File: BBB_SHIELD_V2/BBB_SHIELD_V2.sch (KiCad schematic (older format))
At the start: 6 parts, among them J1 Screw_Terminal_01x04

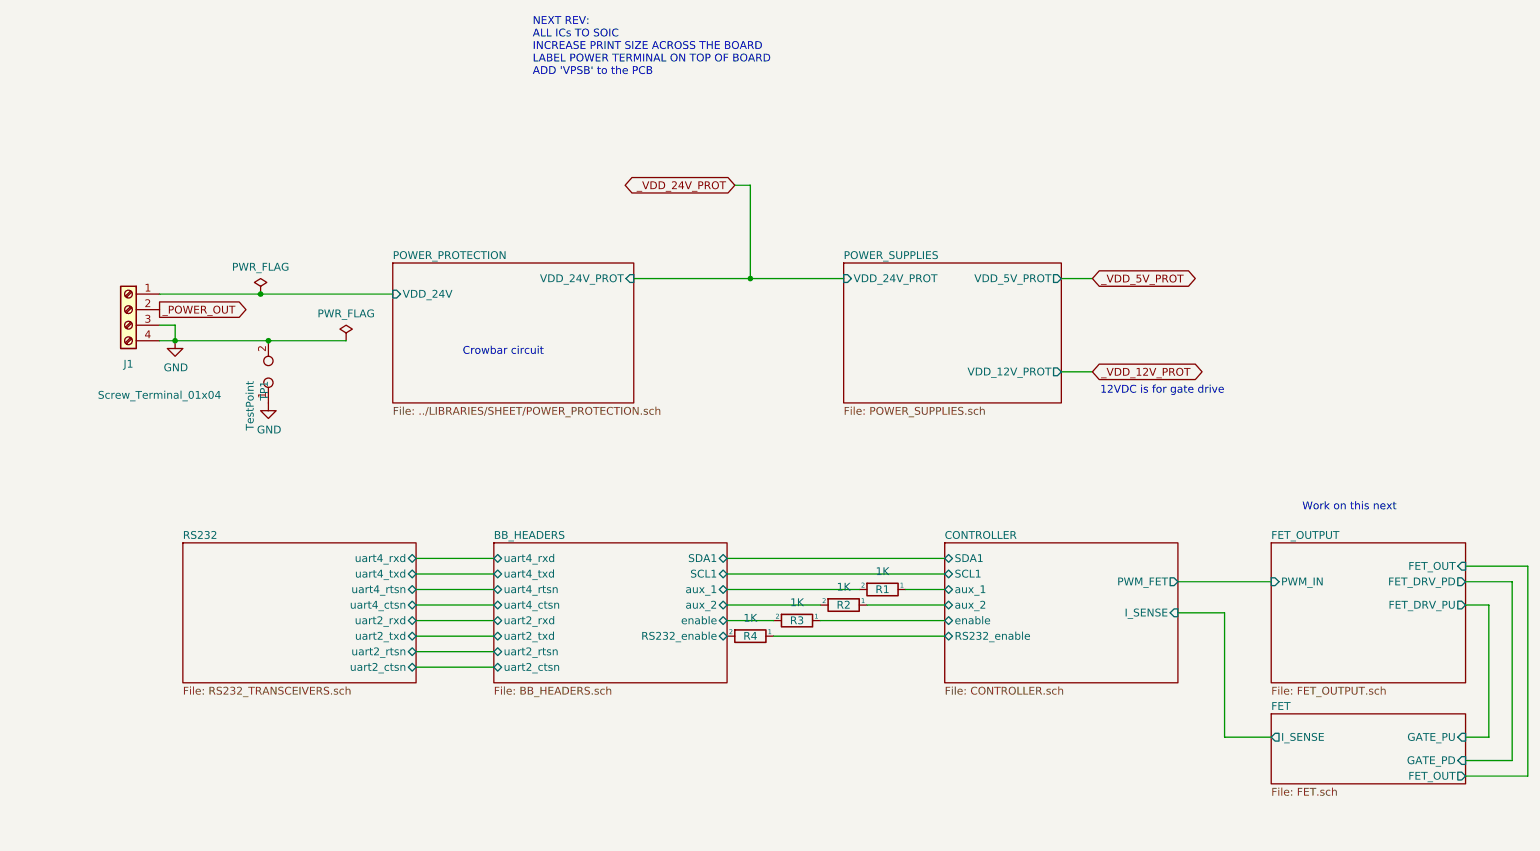
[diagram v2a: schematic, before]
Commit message: Schematics cleanup.  Gerbers for the latest manufacturing release.
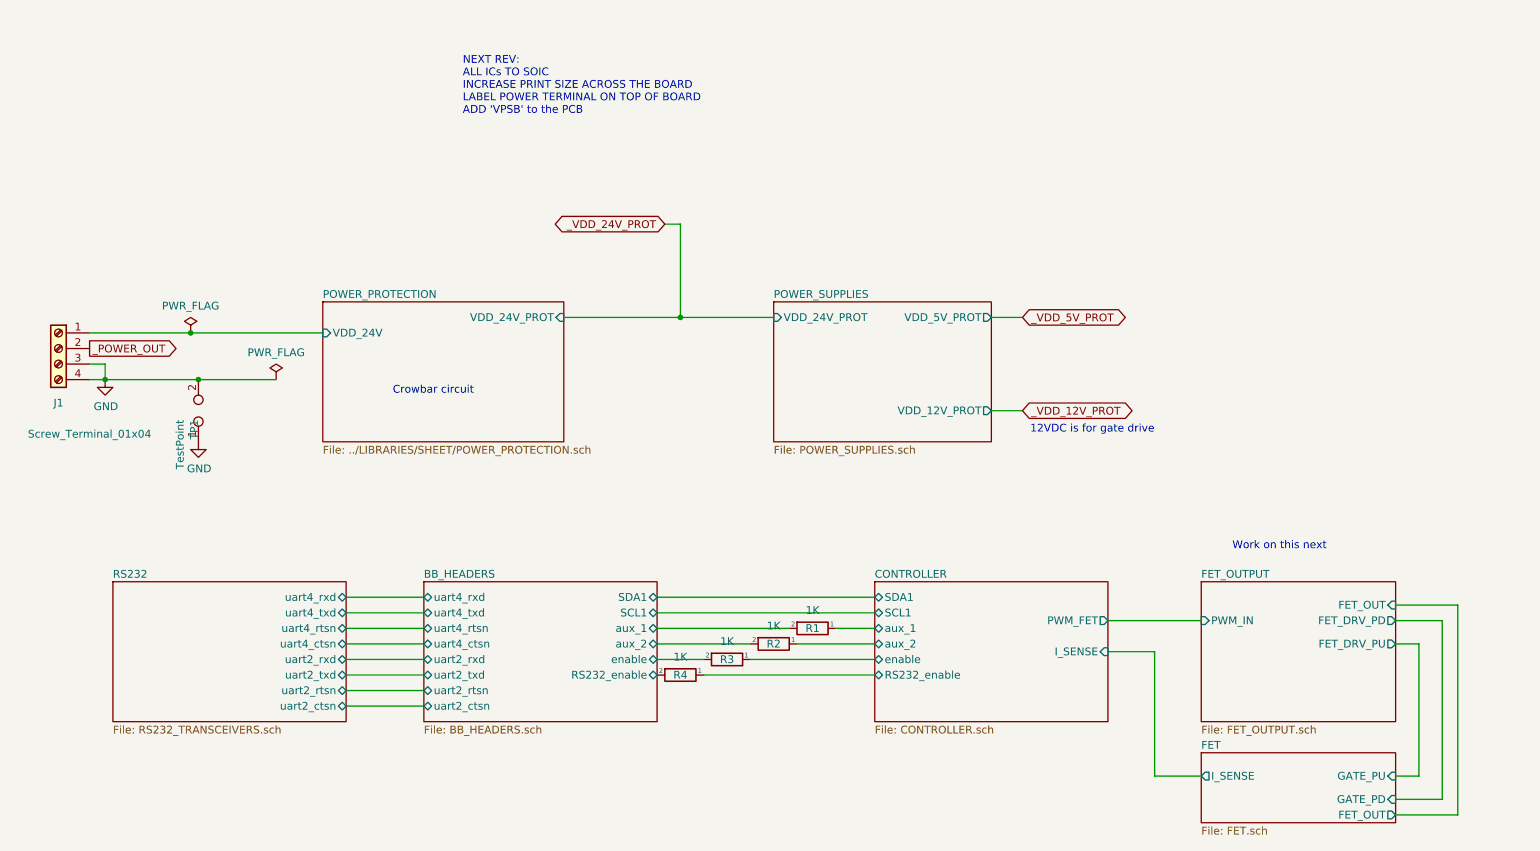
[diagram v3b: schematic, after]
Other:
- moved on the sheet: J1, R1, R2, R3, R4, TP1
